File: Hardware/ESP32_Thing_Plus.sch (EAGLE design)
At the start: 45 parts, among them J1 455-1750-1-ND, J2 USB Female Type C Connector, J3 AUDIO_JACK_TRRSSMD_RA, Q2 MBT3904DW1T1, U2 ESP-WROOM-32NARROW, U3 AP2112K-3.3V, U4 CP2102N, U5 ADMP401

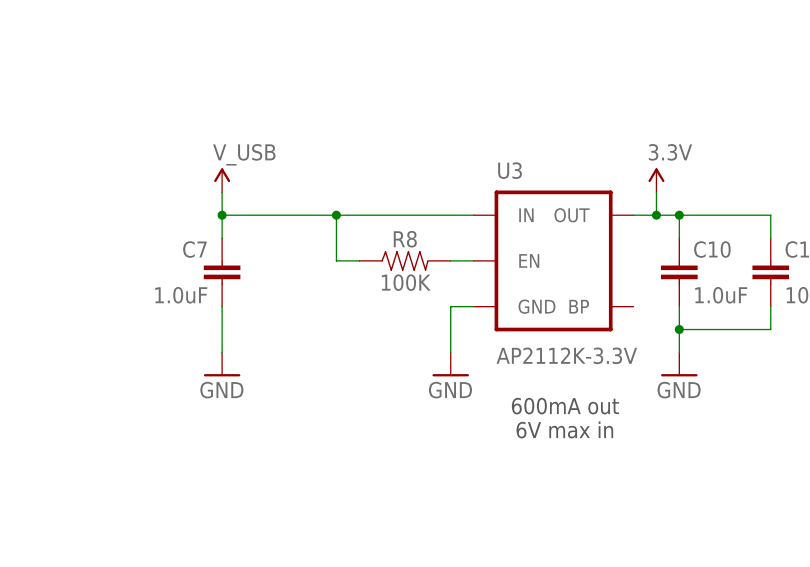
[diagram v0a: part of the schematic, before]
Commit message: changing to 0603
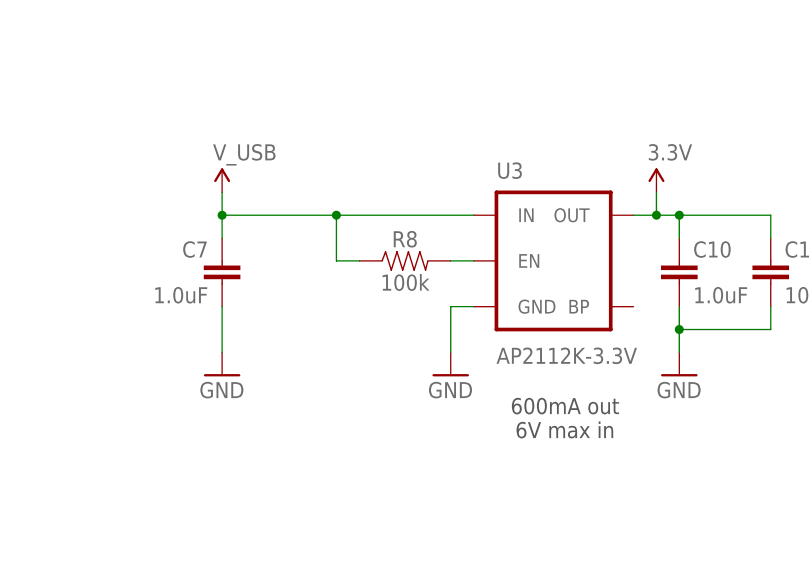
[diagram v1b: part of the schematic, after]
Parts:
- R8: value 100K -> 100k; device SparkFun-Resistors:100KOHM-0402-1/16W-1% -> SparkFun-Resistors:100KOHM-0603-1/10W-1%
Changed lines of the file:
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@@
 <part name="GND3" library="SparkFun-Aesthetics" deviceset="GND" device=""/>
 <part name="C1" library="SparkFun-Capacitors" deviceset="10UF" device="-0603-6.3V-20%" value="10uF"/>
-<part name="R8" library="SparkFun-Resistors" deviceset="100KOHM" device="-0402-1/16W-1%" value="100K"/>
+<part name="R8" library="SparkFun-Resistors" deviceset="100KOHM" device="-0603-1/10W-1%" value="100k"/>
 <part name="FD1" library="SparkFun-Aesthetics" deviceset="FIDUCIAL" device="UFIDUCIAL"/>
 <part name="FD2" library="SparkFun-Aesthetics" deviceset="FIDUCIAL" device="UFIDUCIAL"/>
